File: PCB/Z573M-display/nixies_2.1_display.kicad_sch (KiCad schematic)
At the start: 51 parts, among them Q10 MPSA92, Q11 MPSA42, Q12 MPSA42, Q13 MPSA42, Q14 MPSA42, Q2 MPSA92, Q3 MPSA92, Q4 MPSA92, Q5 MPSA42, Q6 MPSA42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

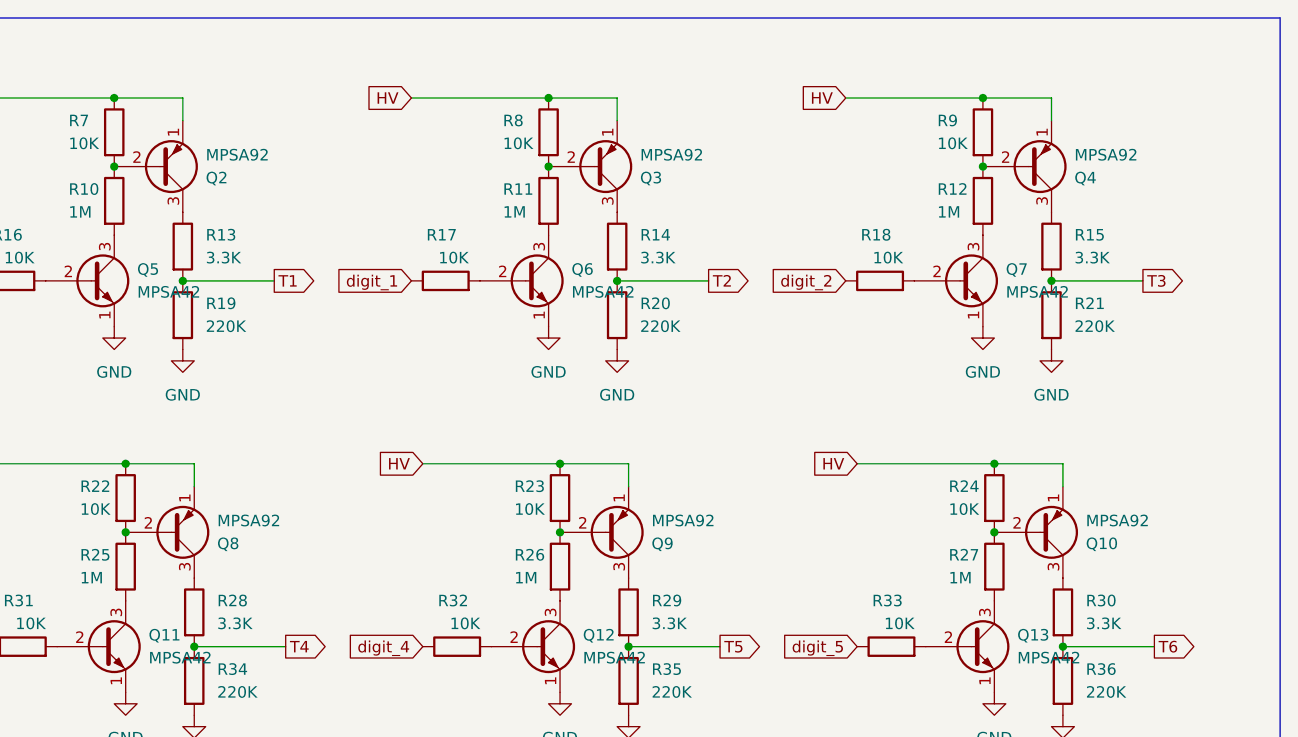
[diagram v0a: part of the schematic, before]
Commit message: New display-only board
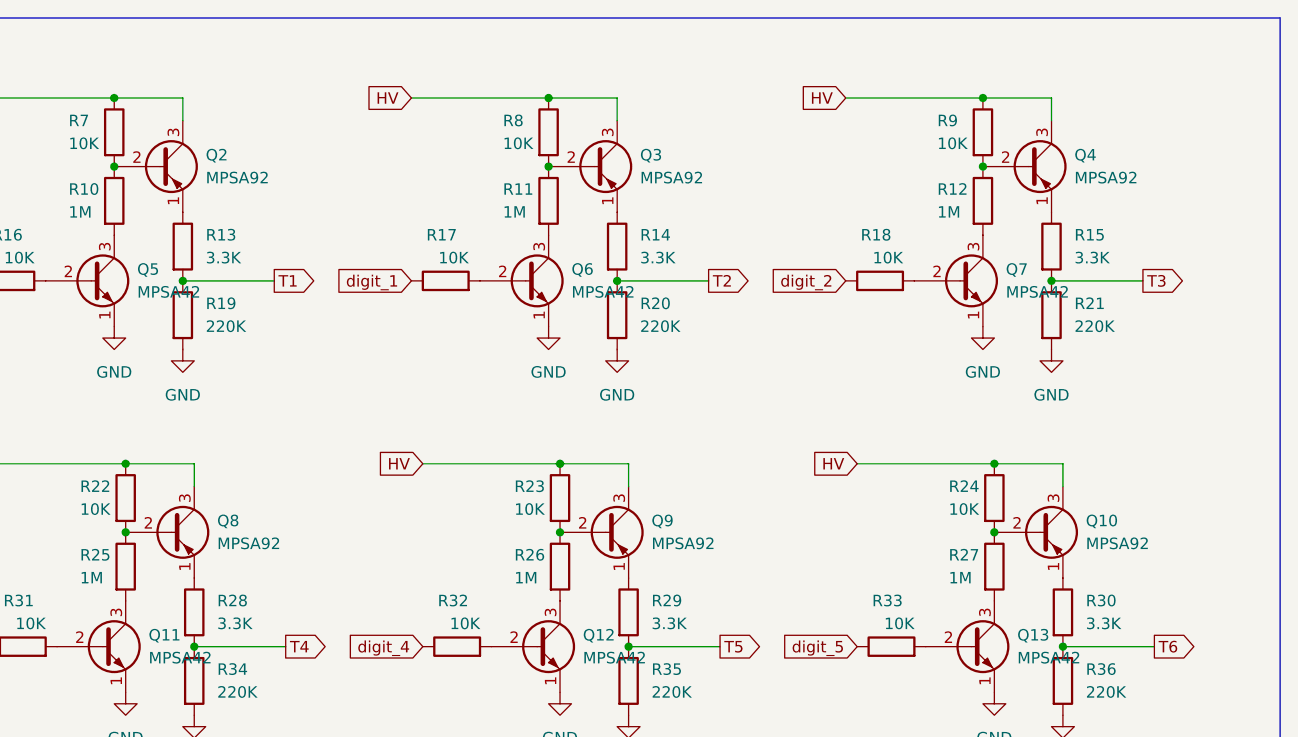
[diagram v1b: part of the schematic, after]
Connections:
- net HV: now also Q10.3 (C), Q2.3 (C), Q3.3 (C), Q4.3 (C), Q8.3 (C), Q9.3 (C); no longer Q10.1 (E), Q2.1 (E), Q3.1 (E), Q4.1 (E), Q8.1 (E), Q9.1 (E)
- net at R14.1: now also Q3.1 (E); no longer Q3.3 (C)
- net at R15.1: now also Q4.1 (E); no longer Q4.3 (C)
- net at R30.1: now also Q10.1 (E); no longer Q10.3 (C)
- net at R29.1: now also Q9.1 (E); no longer Q9.3 (C)
- net at R28.1: now also Q8.1 (E); no longer Q8.3 (C)
- net at R13.1: now also Q2.1 (E); no longer Q2.3 (C)
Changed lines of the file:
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@@
     )
   )
-  (symbol (lib_id "nixie-tube-clock-2.1:MPSA92") (at 229.87 34.29 0) (mirror x) (unit 1)
-    (in_bom yes) (on_board yes) (dnp no)
-    (property "Reference" "Q4" (at 234.95 35.5601 0)
-      (effects (font (size 1.27 1.27)) (justify left))
-    )
-    (property "Value" "MPSA92" (at 234.95 33.0201 0)
-      (effects (font (size 1.27 1.27)) (justify left))
-    )
-    (property "Footprint" "nixie-2.1-footprints:TO-92_HandSolder" (at 234.95 32.385 0)
+  (symbol (lib_id "nixie-tube-clock-2.1:MPSA92") (at 229.87 34.29 0) (unit 1)
+    (in_bom yes) (on_board yes) (dnp no) (fields_autoplaced)
+    (property "Reference" "Q4" (at 234.95 33.0199 0)
+      (effects (font (size 1.27 1.27)) (justify left))
+    )
+    (property "Value" "MPSA92" (at 234.95 35.5599 0)
+      (effects (font (size 1.27 1.27)) (justify left))
+    )
+    (property "Footprint" "nixie-2.1-footprints:TO-92_HandSolder" (at 234.95 36.195 0)
       (effects (font (size 1.27 1.27) italic) (justify left) hide)
     )
@@
     )
   )
-  (symbol (lib_id "nixie-tube-clock-2.1:MPSA92") (at 231.14 74.93 0) (mirror x) (unit 1)
-    (in_bom yes) (on_board yes) (dnp no)
-    (property "Reference" "Q10" (at 236.22 76.2001 0)
-      (effects (font (size 1.27 1.27)) (justify left))
-    )
-    (property "Value" "MPSA92" (at 236.22 73.6601 0)
-      (effects (font (size 1.27 1.27)) (justify left))
-    )
-    (property "Footprint" "nixie-2.1-footprints:TO-92_HandSolder" (at 236.22 73.025 0)
+  (symbol (lib_id "nixie-tube-clock-2.1:MPSA92") (at 231.14 74.93 0) (unit 1)
+    (in_bom yes) (on_board yes) (dnp no) (fields_autoplaced)
+    (property "Reference" "Q10" (at 236.22 73.6599 0)
+      (effects (font (size 1.27 1.27)) (justify left))
+    )
+    (property "Value" "MPSA92" (at 236.22 76.1999 0)
+      (effects (font (size 1.27 1.27)) (justify left))
+    )
+    (property "Footprint" "nixie-2.1-footprints:TO-92_HandSolder" (at 236.22 76.835 0)
       (effects (font (size 1.27 1.27) italic) (justify left) hide)
     )
@@
     )
   )
-  (symbol (lib_id "nixie-tube-clock-2.1:MPSA92") (at 134.62 74.93 0) (mirror x) (unit 1)
-    (in_bom yes) (on_board yes) (dnp no)
-    (property "Reference" "Q8" (at 139.7 76.2001 0)
-      (effects (font (size 1.27 1.27)) (justify left))
-    )
-    (property "Value" "MPSA92" (at 139.7 73.6601 0)
-      (effects (font (size 1.27 1.27)) (justify left))
-    )
-    (property "Footprint" "nixie-2.1-footprints:TO-92_HandSolder" (at 139.7 73.025 0)
+  (symbol (lib_id "nixie-tube-clock-2.1:MPSA92") (at 134.62 74.93 0) (unit 1)
+    (in_bom yes) (on_board yes) (dnp no) (fields_autoplaced)
+    (property "Reference" "Q8" (at 139.7 73.6599 0)
+      (effects (font (size 1.27 1.27)) (justify left))
+    )
+    (property "Value" "MPSA92" (at 139.7 76.1999 0)
+      (effects (font (size 1.27 1.27)) (justify left))
+    )
+    (property "Footprint" "nixie-2.1-footprints:TO-92_HandSolder" (at 139.7 76.835 0)
       (effects (font (size 1.27 1.27) italic) (justify left) hide)
     )
@@
     )
   )
-  (symbol (lib_id "nixie-tube-clock-2.1:MPSA92") (at 181.61 34.29 0) (mirror x) (unit 1)
-    (in_bom yes) (on_board yes) (dnp no)
-    (property "Reference" "Q3" (at 186.69 35.5601 0)
-      (effects (font (size 1.27 1.27)) (justify left))
-    )
-    (property "Value" "MPSA92" (at 186.69 33.0201 0)
-      (effects (font (size 1.27 1.27)) (justify left))
-    )
-    (property "Footprint" "nixie-2.1-footprints:TO-92_HandSolder" (at 186.69 32.385 0)
+  (symbol (lib_id "nixie-tube-clock-2.1:MPSA92") (at 181.61 34.29 0) (unit 1)
+    (in_bom yes) (on_board yes) (dnp no) (fields_autoplaced)
+    (property "Reference" "Q3" (at 186.69 33.0199 0)
+      (effects (font (size 1.27 1.27)) (justify left))
+    )
+    (property "Value" "MPSA92" (at 186.69 35.5599 0)
+      (effects (font (size 1.27 1.27)) (justify left))
+    )
+    (property "Footprint" "nixie-2.1-footprints:TO-92_HandSolder" (at 186.69 36.195 0)
       (effects (font (size 1.27 1.27) italic) (justify left) hide)
     )
@@
     )
   )
-  (symbol (lib_id "nixie-tube-clock-2.1:MPSA92") (at 133.35 34.29 0) (mirror x) (unit 1)
-    (in_bom yes) (on_board yes) (dnp no)
-    (property "Reference" "Q2" (at 138.43 35.5601 0)
-      (effects (font (size 1.27 1.27)) (justify left))
-    )
-    (property "Value" "MPSA92" (at 138.43 33.0201 0)
-      (effects (font (size 1.27 1.27)) (justify left))
-    )
-    (property "Footprint" "nixie-2.1-footprints:TO-92_HandSolder" (at 138.43 32.385 0)
+  (symbol (lib_id "nixie-tube-clock-2.1:MPSA92") (at 133.35 34.29 0) (unit 1)
+    (in_bom yes) (on_board yes) (dnp no) (fields_autoplaced)
+    (property "Reference" "Q2" (at 138.43 33.0199 0)
+      (effects (font (size 1.27 1.27)) (justify left))
+    )
+    (property "Value" "MPSA92" (at 138.43 35.5599 0)
+      (effects (font (size 1.27 1.27)) (justify left))
+    )
+    (property "Footprint" "nixie-2.1-footprints:TO-92_HandSolder" (at 138.43 36.195 0)
       (effects (font (size 1.27 1.27) italic) (justify left) hide)
     )
@@
     )
   )
-  (symbol (lib_id "nixie-tube-clock-2.1:MPSA92") (at 182.88 74.93 0) (mirror x) (unit 1)
-    (in_bom yes) (on_board yes) (dnp no)
-    (property "Reference" "Q9" (at 187.96 76.2001 0)
-      (effects (font (size 1.27 1.27)) (justify left))
-    )
-    (property "Value" "MPSA92" (at 187.96 73.6601 0)
-      (effects (font (size 1.27 1.27)) (justify left))
-    )
-    (property "Footprint" "nixie-2.1-footprints:TO-92_HandSolder" (at 187.96 73.025 0)
+  (symbol (lib_id "nixie-tube-clock-2.1:MPSA92") (at 182.88 74.93 0) (unit 1)
+    (in_bom yes) (on_board yes) (dnp no) (fields_autoplaced)
+    (property "Reference" "Q9" (at 187.96 73.6599 0)
+      (effects (font (size 1.27 1.27)) (justify left))
+    )
+    (property "Value" "MPSA92" (at 187.96 76.1999 0)
+      (effects (font (size 1.27 1.27)) (justify left))
+    )
+    (property "Footprint" "nixie-2.1-footprints:TO-92_HandSolder" (at 187.96 76.835 0)
       (effects (font (size 1.27 1.27) italic) (justify left) hide)
     )
